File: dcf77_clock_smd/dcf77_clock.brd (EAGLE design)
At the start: 83.5 x 76.2 mm, 24 parts, among them IC1 7805DT, IC2 ATMEGA48/88/168-AU, J2 DCJ0202, U1 LCD-16X2SILK

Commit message: Update
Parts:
- moved C2 21.7 mm to (57.1, 53.3)
- moved D1 1.80 mm to (43.2, 39.4)
- moved SG2 1.27 mm to (49.5, 45.7)
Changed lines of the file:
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@@
 <attribute name="VALUE" x="59.944" y="56.134" size="1.27" layer="27" ratio="10" rot="R90"/>
 </element>
-<element name="C2" library="rcl" library_urn="urn:adsk.eagle:library:334" package="E2-5" package3d_urn="urn:adsk.eagle:package:23346/2" value="" x="78.74" y="55.88" smashed="yes">
-<attribute name="NAME" x="81.28" y="56.896" size="1.27" layer="25" ratio="10"/>
-<attribute name="POPULARITY" value="14" x="163.83" y="-53.34" size="1.778" layer="27" display="off"/>
-<attribute name="SPICEPREFIX" value="C" x="163.83" y="-53.34" size="1.778" layer="27" display="off"/>
-<attribute name="VALUE" x="81.28" y="53.721" size="1.27" layer="27" ratio="10"/>
+<element name="C2" library="rcl" library_urn="urn:adsk.eagle:library:334" package="E2-5" package3d_urn="urn:adsk.eagle:package:23346/2" value="" x="57.15" y="53.34" smashed="yes">
+<attribute name="NAME" x="59.69" y="54.356" size="1.27" layer="25" ratio="10"/>
+<attribute name="POPULARITY" value="14" x="142.24" y="-55.88" size="1.778" layer="27" display="off"/>
+<attribute name="SPICEPREFIX" value="C" x="142.24" y="-55.88" size="1.778" layer="27" display="off"/>
+<attribute name="VALUE" x="59.69" y="51.181" size="1.27" layer="27" ratio="10"/>
 </element>
-<element name="D1" library="diode" library_urn="urn:adsk.eagle:library:210" package="SOD123" package3d_urn="urn:adsk.eagle:package:43420/1" value="1N4007" x="44.45" y="40.64" smashed="yes" rot="R180">
-<attribute name="NAME" x="46.482" y="38.989" size="1.27" layer="25" ratio="10" rot="R180"/>
-<attribute name="POPULARITY" value="22" x="44.45" y="40.64" size="1.778" layer="27" rot="R180" display="off"/>
-<attribute name="VALUE" x="46.482" y="43.561" size="1.27" layer="27" ratio="10" rot="R180"/>
+<element name="D1" library="diode" library_urn="urn:adsk.eagle:library:210" package="SOD123" package3d_urn="urn:adsk.eagle:package:43420/1" value="1N4007" x="43.18" y="39.37" smashed="yes" rot="R180">
+<attribute name="NAME" x="45.212" y="37.719" size="1.27" layer="25" ratio="10" rot="R180"/>
+<attribute name="POPULARITY" value="22" x="43.18" y="39.37" size="1.778" layer="27" rot="R180" display="off"/>
+<attribute name="VALUE" x="45.212" y="42.291" size="1.27" layer="27" ratio="10" rot="R180"/>
 </element>
 <element name="EN1" library="bourns" package="PEC11_4XXXXK-S" value="PEC11" x="58.42" y="45.72" smashed="yes" rot="R270">
@@
 <attribute name="VALUE" x="37.6174" y="46.0756" size="0.9906" layer="27" ratio="10" rot="R270"/>
 </element>
-<element name="SG2" library="SparkFun" package="BUZZER-CCV-KIT" value="LD-BZEN-1201" x="50.8" y="45.72" smashed="yes">
-<attribute name="NAME" x="55.245" y="52.705" size="1.27" layer="25" ratio="10"/>
-<attribute name="VALUE" x="46.355" y="41.91" size="1.27" layer="27" ratio="10"/>
+<element name="SG2" library="SparkFun" package="BUZZER-CCV-KIT" value="LD-BZEN-1201" x="49.53" y="45.72" smashed="yes">
+<attribute name="NAME" x="53.975" y="52.705" size="1.27" layer="25" ratio="10"/>
+<attribute name="VALUE" x="45.085" y="41.91" size="1.27" layer="27" ratio="10"/>
 </element>
 <element name="U$1" library="SparkFun" package="2X5-SHROUDED" value="AVR_SPI_PROG2PTH2" x="78.74" y="57.15" smashed="yes">

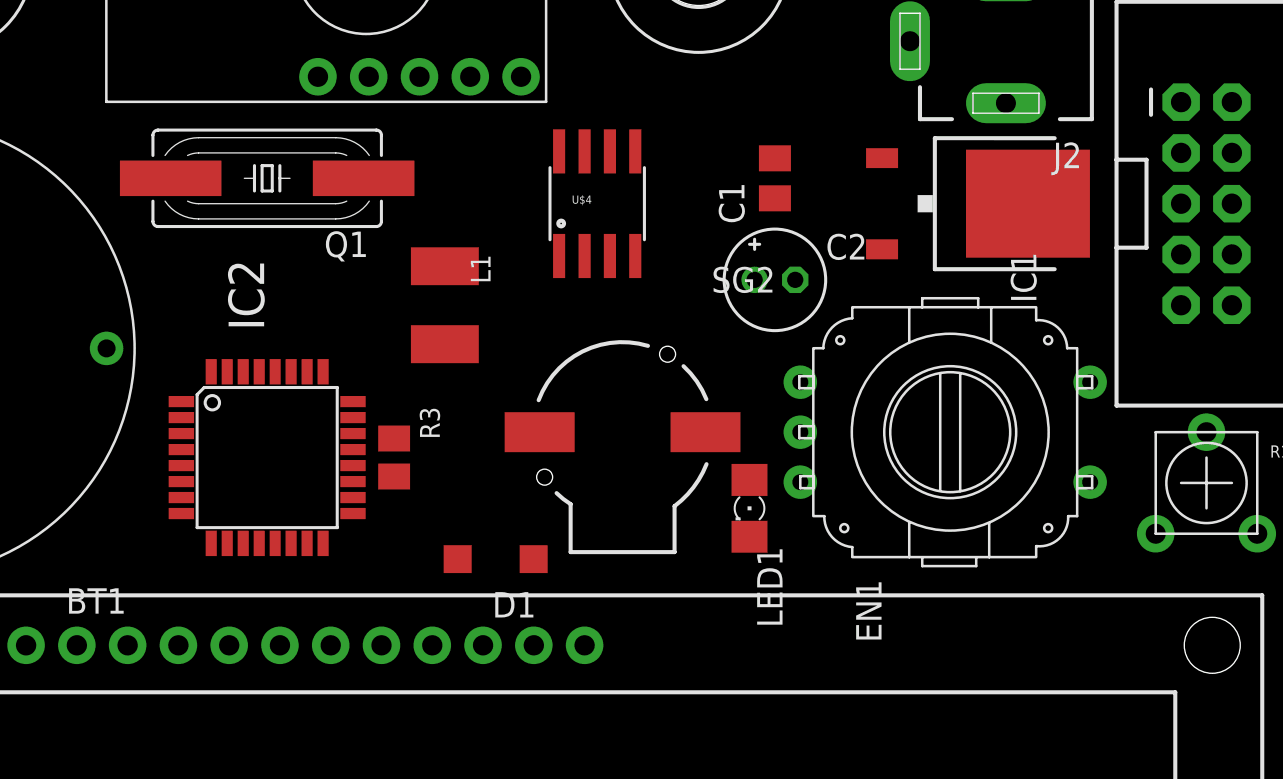
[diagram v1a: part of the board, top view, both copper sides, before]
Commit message: Update capacitors footprints
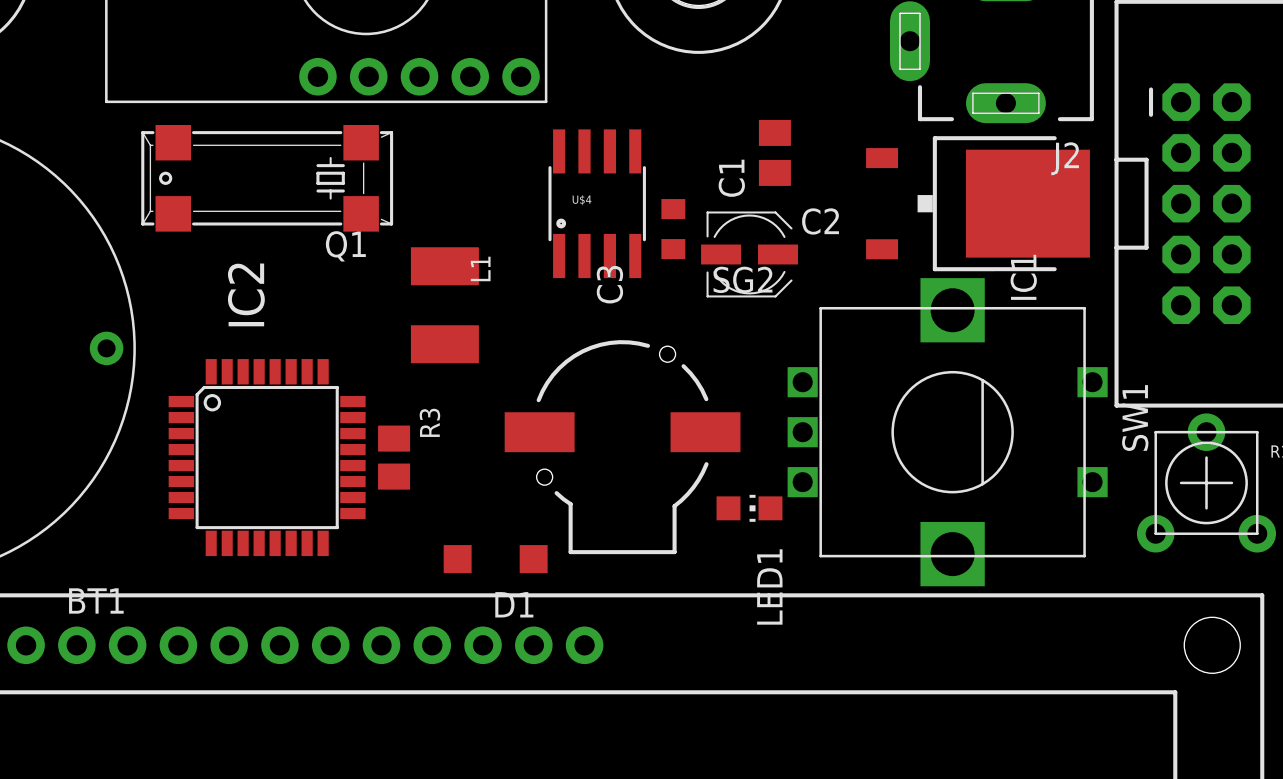
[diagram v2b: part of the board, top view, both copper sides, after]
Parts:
- removed EN1: PEC11, bourns:PEC11_4XXXXK-S
- added C3: (no value), rcl:SMC_Z
- added SW1: EC12E_SW, switch-alps:ALPS_EC12E_SW
- C2: device rcl:E2-5 -> rcl:UD-4X5,8_NICHICON
- LED1: device SparkFun:FKIT-LED-1206 -> led:CHIP-LED0805
- Q1: device crystal:SM49 -> crystal:MM39SL
- moved C2 1.80 mm to (55.9, 54.6)
- moved C1 1.27 mm to (57.1, 59.7)
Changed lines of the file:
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@@
 <attribute name="VALUE" x="24.716" y="62.911" size="1.27" layer="27" rot="R180"/>
 </element>
-<element name="C1" library="rcl" library_urn="urn:adsk.eagle:library:334" package="C0805K" package3d_urn="urn:adsk.eagle:package:23681/2" value="100n" x="57.15" y="58.42" smashed="yes" rot="R90">
-<attribute name="NAME" x="55.626" y="56.134" size="1.27" layer="25" ratio="10" rot="R90"/>
-<attribute name="POPULARITY" value="52" x="57.15" y="58.42" size="1.778" layer="27" rot="R90" display="off"/>
-<attribute name="SPICEPREFIX" value="C" x="57.15" y="58.42" size="1.778" layer="27" rot="R90" display="off"/>
-<attribute name="VALUE" x="59.944" y="56.134" size="1.27" layer="27" ratio="10" rot="R90"/>
+<element name="C1" library="rcl" library_urn="urn:adsk.eagle:library:334" package="C0805K" package3d_urn="urn:adsk.eagle:package:23681/2" value="100n" x="57.15" y="59.69" smashed="yes" rot="R90">
+<attribute name="NAME" x="55.626" y="57.404" size="1.27" layer="25" ratio="10" rot="R90"/>
+<attribute name="POPULARITY" value="52" x="57.15" y="59.69" size="1.778" layer="27" rot="R90" display="off"/>
+<attribute name="SPICEPREFIX" value="C" x="57.15" y="59.69" size="1.778" layer="27" rot="R90" display="off"/>
+<attribute name="VALUE" x="59.944" y="57.404" size="1.27" layer="27" ratio="10" rot="R90"/>
 </element>
-<element name="C2" library="rcl" library_urn="urn:adsk.eagle:library:334" package="E2-5" package3d_urn="urn:adsk.eagle:package:23346/2" value="" x="57.15" y="53.34" smashed="yes">
-<attribute name="NAME" x="59.69" y="54.356" size="1.27" layer="25" ratio="10"/>
-<attribute name="POPULARITY" value="14" x="142.24" y="-55.88" size="1.778" layer="27" display="off"/>
-<attribute name="SPICEPREFIX" value="C" x="142.24" y="-55.88" size="1.778" layer="27" display="off"/>
-<attribute name="VALUE" x="59.69" y="51.181" size="1.27" layer="27" ratio="10"/>
+<element name="C2" library="rcl" library_urn="urn:adsk.eagle:library:334" package="UD-4X5,8_NICHICON" package3d_urn="urn:adsk.eagle:package:23474/1" value="" x="55.88" y="54.61" smashed="yes">
+<attribute name="NAME" x="58.42" y="55.626" size="1.27" layer="25" ratio="10"/>
+<attribute name="POPULARITY" value="0" x="140.97" y="-54.61" size="1.778" layer="27" display="off"/>
+<attribute name="SPICEPREFIX" value="C" x="140.97" y="-54.61" size="1.778" layer="27" display="off"/>
+<attribute name="VALUE" x="58.42" y="52.451" size="1.27" layer="27" ratio="10"/>
 </element>
 <element name="D1" library="diode" library_urn="urn:adsk.eagle:library:210" package="SOD123" package3d_urn="urn:adsk.eagle:package:43420/1" value="1N4007" x="43.18" y="39.37" smashed="yes" rot="R180">
@@
 <attribute name="POPULARITY" value="22" x="43.18" y="39.37" size="1.778" layer="27" rot="R180" display="off"/>
 <attribute name="VALUE" x="45.212" y="42.291" size="1.27" layer="27" ratio="10" rot="R180"/>
-</element>
-<element name="EN1" library="bourns" package="PEC11_4XXXXK-S" value="PEC11" x="58.42" y="45.72" smashed="yes" rot="R270">
-<attribute name="NAME" x="61.214" y="38.353996875" size="1.27" layer="25" rot="R270"/>
-<attribute name="VALUE" x="59.69" y="38.09999375" size="1.27" layer="27" rot="R270"/>
 </element>
 <element name="H1" library="holes" library_urn="urn:adsk.eagle:library:237" package="3,2" package3d_urn="urn:adsk.eagle:package:14275/1" value="MOUNT-HOLE3.2" x="4.191" y="71.755" smashed="yes">
@@
 <attribute name="VALUE" x="40.1574" y="53.6956" size="0.9906" layer="27" ratio="10" rot="R270"/>
 </element>
-<element name="LED1" library="SparkFun" package="FKIT-LED-1206" value="" x="55.88" y="41.91" smashed="yes" rot="R270">
+<element name="LED1" library="led" library_urn="urn:adsk.eagle:library:259" package="CHIP-LED0805" package3d_urn="urn:adsk.eagle:package:15818/2" value="" x="55.88" y="41.91" smashed="yes" rot="R270">
 <attribute name="NAME" x="56.261" y="40.005" size="1.27" layer="25" ratio="10" rot="R270"/>
+<attribute name="POPULARITY" value="68" x="55.88" y="41.91" size="1.778" layer="27" rot="R270" display="off"/>
 <attribute name="VALUE" x="54.229" y="40.005" size="1.27" layer="27" ratio="10" rot="R270"/>
 </element>
@@
 <attribute name="NAME" x="23.45" y="76.5" size="1.27" layer="25"/>
 </element>
-<element name="Q1" library="crystal" library_urn="urn:adsk.eagle:library:204" package="SM49" package3d_urn="urn:adsk.eagle:package:12085/1" value="" x="31.75" y="58.42" smashed="yes" rot="R180">
+<element name="Q1" library="crystal" library_urn="urn:adsk.eagle:library:204" package="MM39SL" package3d_urn="urn:adsk.eagle:package:12090/1" value="" x="31.75" y="58.42" smashed="yes" rot="R180">
 <attribute name="MF" value="" x="31.75" y="58.42" size="1.778" layer="27" rot="R180" display="off"/>
 <attribute name="MPN" value="" x="31.75" y="58.42" size="1.778" layer="27" rot="R180" display="off"/>
@@
 <attribute name="OC_FARNELL" value="unknown" x="31.75" y="58.42" size="1.778" layer="27" rot="R180" display="off"/>
 <attribute name="OC_NEWARK" value="unknown" x="31.75" y="58.42" size="1.778" layer="27" rot="R180" display="off"/>
-<attribute name="POPULARITY" value="3" x="-35.56" y="167.64" size="1.778" layer="27" rot="R180" display="off"/>
+<attribute name="POPULARITY" value="0" x="-35.56" y="167.64" size="1.778" layer="27" rot="R180" display="off"/>
 <attribute name="VALUE" x="36.83" y="62.357" size="1.27" layer="27" ratio="10" rot="R180"/>
 </element>
@@
 </element>
 <element name="U1" library="SparkFun" package="LCD-16X2" value="LCD-16X2SILK" x="41.529" y="19.558" smashed="yes"/>
+<element name="SW1" library="switch-alps" library_urn="urn:adsk.eagle:library:373" package="ALPS_EC12E_SW" package3d_urn="urn:adsk.eagle:package:27083/1" value="EC12E_SW" x="66.04" y="45.72" smashed="yes" rot="R270">
+<attribute name="MF" value="" x="66.04" y="45.72" size="1.778" layer="27" rot="R270" display="off"/>
+<attribute name="MPN" value="EC12E2424407" x="66.04" y="45.72" size="1.778" layer="27" rot="R270" display="off"/>
+<attribute name="NAME" x="74.54" y="48.22" size="1.27" layer="25" rot="R270"/>
+<attribute name="OC_FARNELL" value="1520813" x="66.04" y="45.72" size="1.778" layer="27" rot="R270" display="off"/>
+<attribute name="OC_NEWARK" value="74M1068" x="66.04" y="45.72" size="1.778" layer="27" rot="R270" display="off"/>
+<attribute name="POPULARITY" value="3" x="66.04" y="45.72" size="1.778" layer="27" rot="R270" display="off"/>
+<attribute name="VALUE" x="57.04" y="42.22" size="1.27" layer="27" rot="R90"/>
+</element>
+<element name="C3" library="rcl" library_urn="urn:adsk.eagle:library:334" package="SMC_Z" package3d_urn="urn:adsk.eagle:package:25927/3" value="" x="52.07" y="55.88" smashed="yes" rot="R90">
+<attribute name="NAME" x="49.53" y="52.07" size="1.27" layer="25" rot="R90"/>
+<attribute name="POPULARITY" value="0" x="52.07" y="55.88" size="1.778" layer="27" rot="R90" display="off"/>
+<attribute name="SPICEPREFIX" value="C" x="52.07" y="55.88" size="1.778" layer="27" rot="R90" display="off"/>
+<attribute name="VALUE" x="55.88" y="52.07" size="1.27" layer="27" rot="R90"/>
+</element>
 </elements>
 <signals>

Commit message: Add power supply and basic components schematic
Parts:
- removed L1: (no value), rcl:L1812
- added C4, C5, C6: 100n, rcl:C0805K
- added Q2: IRLML6244TRPBF, sosbutton:SOT23
- added R2, R6: 10k, rcl:M0805
- added R4: 1k, rcl:M0805
- added R5: 100R, rcl:M0805
- C2: value (none) -> 22uF
- C3: value (none) -> 0.22uF
- moved C2 16.9 mm to (39.4, 50.8)
- moved C3 10.9 mm to (61.0, 62.2)
- moved C1 4.02 mm to (58.4, 55.9)
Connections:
- removed net AGND: IC2.21
- new net BUZZER_PWM: R4.1
- new net ISP_MISO: IC2.16, U$1.9
- new net ISP_MOSI: IC2.15, U$1.1
- new net ISP_SCK: IC2.17, U$1.7
- new net LED: R5.2
- new net MCU_RX: IC2.30, U$1.4
- new net MCU_TX: IC2.31, U$1.6
- new net N$1: C3.+, IC1.1, J2.1
- new net N$2: D1.A, Q2.3, SG2.-
- new net N$3: Q2.1, R2.2, R4.2
- new net N$4: LED1.A, R5.1
- new net N$8: IC2.14
- new net RESET: IC2.29, R3.2, U$1.5
- new net SW: C6.1, R6.1, SW1.E
- net GND: now also C1.2, C2.-, C3.-, C4.2, C5.2, C6.2, IC1.3, IC2.21, J2.2, J2.3, LED1.C, Q2.2, R2.1, SW1.D, U$1.10, U$1.8
- net VCC: now also C1.1, C2.+, C4.1, C5.1, D1.C, IC1.2, IC2.18, R3.1, R6.2, SG2.+, U$1.2

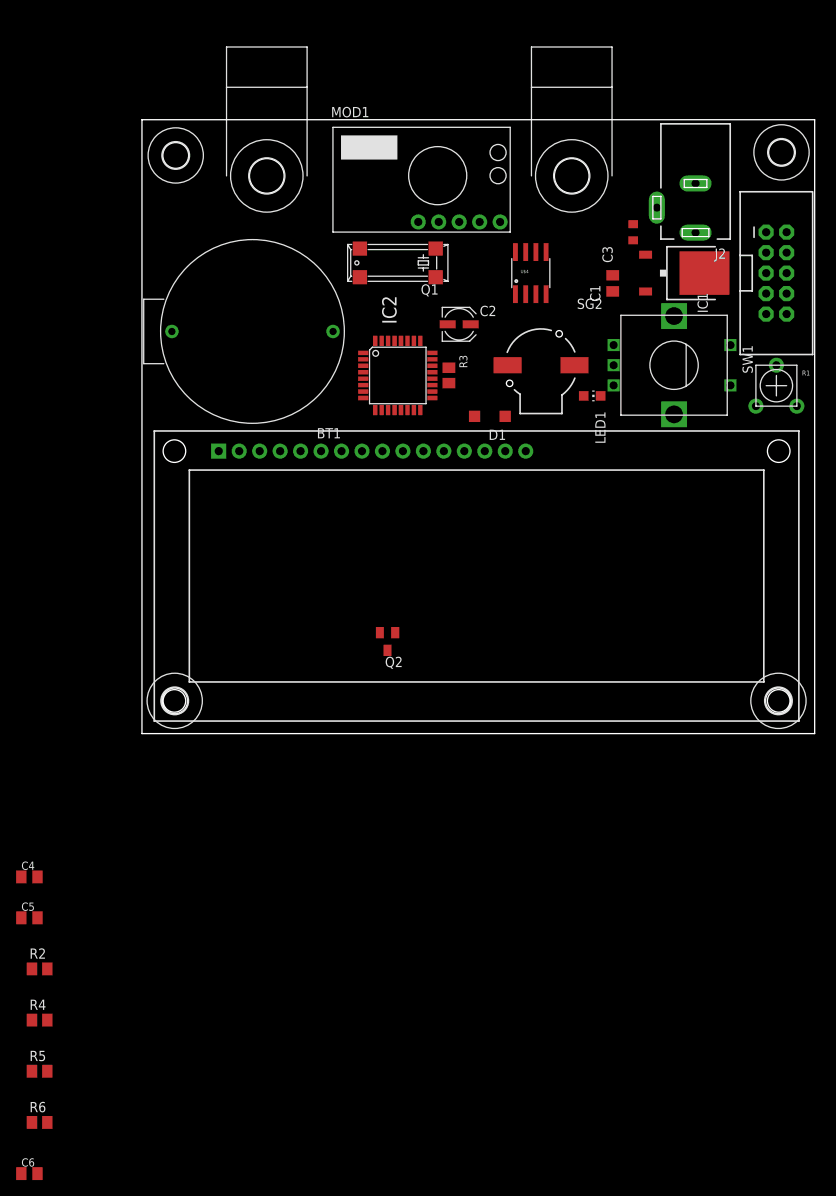
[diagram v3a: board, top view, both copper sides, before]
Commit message: Add first complete version of schematic
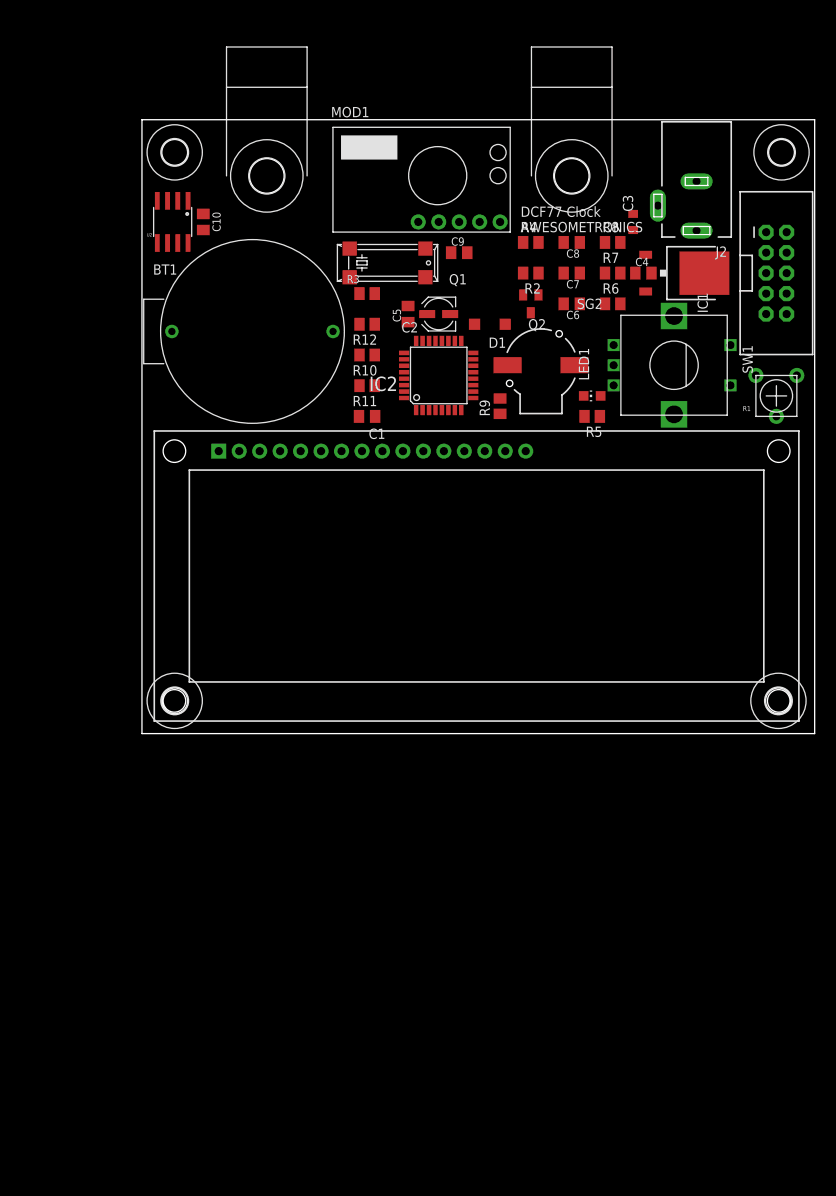
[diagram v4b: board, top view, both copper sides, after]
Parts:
- removed U$4: DS1307SO8, SparkFun:SO08
- added C10, C7, C8, C9: 100n, rcl:C0805K
- added R10, R11, R12: 4.7k, rcl:M0805
- added R7, R8: 10k, rcl:M0805
- added R9: 100R, rcl:M0805
- added U2: DS1307SO8, SparkFun:SO08
- R1: value TRIMPOTPTH -> 10k
- moved C6 127.2 mm to (53.3, 53.3), turned to 180 degrees
- moved R6 124.0 mm to (58.4, 53.3)
- moved R4 114.2 mm to (48.3, 61.0)
- moved C4 106.9 mm to (62.2, 57.1)
- moved R5 106.3 mm to (55.9, 39.4), turned to 180 degrees
- moved R2 105.7 mm to (48.3, 57.1), turned to 180 degrees
- moved C5 88.4 mm to (33.0, 52.1), turned to 90 degrees
- moved Q2 45.5 mm to (48.3, 53.3)
- moved C1 34.7 mm to (27.9, 39.4), turned to 180 degrees
- moved R3 14.4 mm to (27.9, 54.6), turned to 0 degrees
- moved D1 11.4 mm to (43.2, 50.8)
- moved IC2 5.08 mm to (36.8, 44.5), turned to 90 degrees
- moved C2 2.84 mm to (36.8, 52.1), turned to 180 degrees
- moved C3 1.27 mm to (61.0, 63.5)
- moved R1 1.27 mm to (78.7, 41.9), turned to 180 degrees
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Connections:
- removed net A: U1.15
- removed net BUZZER_PWM: R4.1
- removed net ISP_MOSI: IC2.15, U$1.1
- removed net K: U1.16
- removed net VDD: U1.2
- removed net VSS: U1.1
- new net DCF77_OUT: IC2.12, MOD1.P$2
- new net DCF77_SEL: IC2.13, MOD1.P$1
- new net ENC_A: C7.1, IC2.32, R7.1, SW1.A
- new net ENC_B: C8.1, IC2.1, R8.1, SW1.B
- new net ISP_MOSI_BUZ_PWM: IC2.15, R4.1, U$1.1
- new net LCD_DB4: IC2.7, U1.11
- new net LCD_DB5: IC2.8, U1.12
- new net LCD_DB6: IC2.9, U1.13
- new net LCD_DB7: IC2.11, U1.14
- new net LCD_E: IC2.2, U1.6
- new net LCD_RS: IC2.25, U1.4
- new net N$10: Q1.1, U2.1
- new net N$11: Q1.4, U2.2
- new net N$12: BT1.P$2, U2.3
- new net N$7: R1.2, U1.3
- new net N$9: R9.1, U1.16
- new net RTC_SCL: IC2.28, R11.2, U2.6
- new net RTC_SDA: IC2.27, R12.2, U2.5
- new net RTC_SQW: IC2.26, R10.2, U2.7
- net GND: now also BT1.P$1, C10.2, C7.2, C8.2, C9.2, MOD1.P$4, R1.3, R9.2, SW1.C, U1.1, U1.5, U2.4
- net LED: now also IC2.10
- net SW: now also IC2.19
- net VCC: now also C10.1, C9.1, MOD1.P$5, R1.1, R10.1, R11.1, R12.1, R7.2, R8.2, U1.15, U1.2, U2.8
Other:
- board text added: "DCF77 Clock AWESOMETRONICS"
